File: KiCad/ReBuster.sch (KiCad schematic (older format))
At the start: 11 parts, among them U3 SN74CBTD16210, U4 SN74LVC16T245DGVR, U5 SN74CBTD16210, U6 SN74CBTD16210, U7 74LVC2T45DC, U8 PLCC_84_plug, U9 PLCC_84_plug

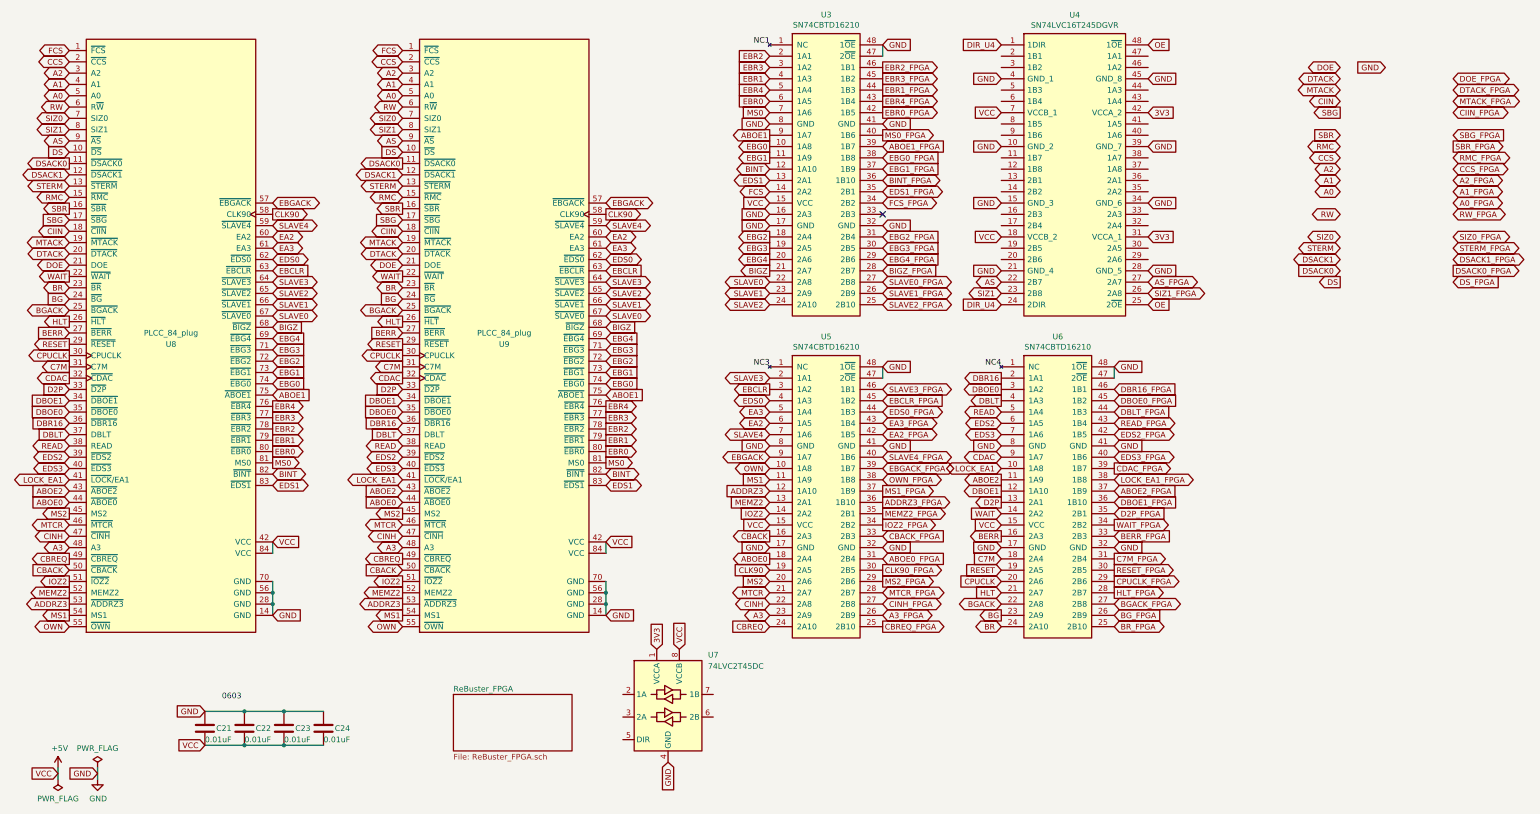
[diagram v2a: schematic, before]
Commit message: Route AS,SIZ1,SIZ0,RW to U4 (SN74LVC16T245DGVR) and FPGA
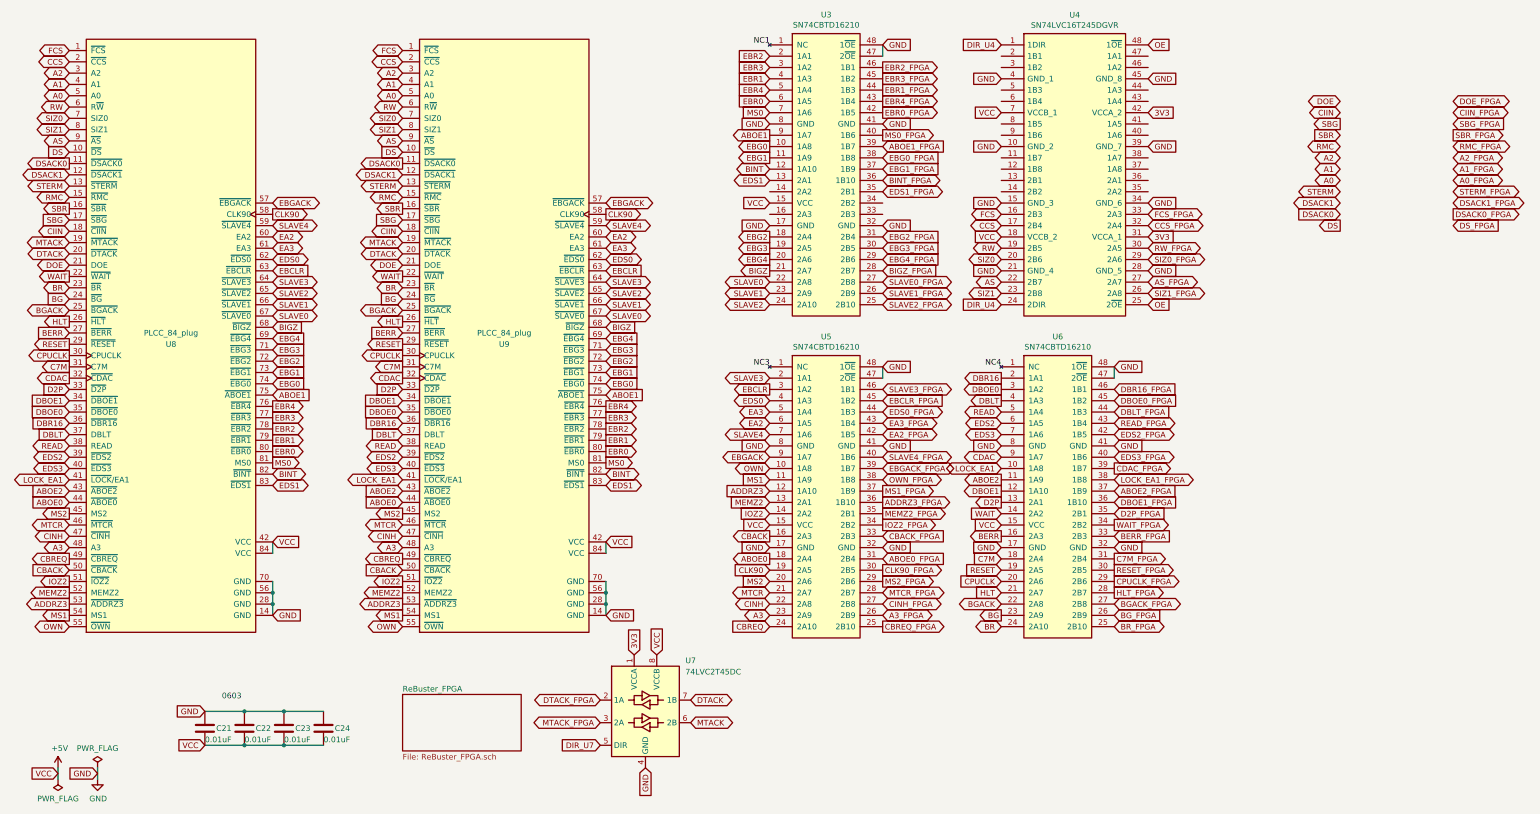
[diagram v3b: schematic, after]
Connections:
- net CCS: now also U4.17 (2B4)
- net CCS_FPGA: now also U4.32 (2A4)
- net DTACK: now also U7.7 (1B)
- net DTACK_FPGA: now also U7.2 (1A)
- net FCS: now also U4.16 (2B3); no longer U3.14 (2A2)
- net FCS_FPGA: now also U4.33 (2A3); no longer U3.34 (2B2)
- net GND: no longer U3.16 (2A3)
- net MTACK: now also U7.6 (2B)
- net MTACK_FPGA: now also U7.3 (2A)
- net RW: now also U4.19 (2B5)
- net RW_FPGA: now also U4.30 (2A5)
- net SIZ0: now also U4.20 (2B6)
- net SIZ0_FPGA: now also U4.29 (2A6)
- net DIR_U7: now reaches U7.5 (DIR)
- no-connect marks 1 -> 0
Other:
- moved on the sheet: U7
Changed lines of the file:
@@
 Wire Wire Line
 	8150 3900 8150 3800
-$Comp
-L ReBuster:SN74CBTD16210 U3
-U 1 1 6058DC08
-P 7650 2050
-F 0 "U3" H 7650 3417 50  0000 C CNN
-F 1 "SN74CBTD16210" H 7650 3326 50  0000 C CNN
-F 2 "ReBuster:TSSOP-48_6.1x12.5mm_P0.5mm_padLength_1mm" H 9300 2500 50  0001 C CNN
-F 3 "https://www.ti.com/lit/ds/symlink/sn74cbtd16210.pdf" H 9300 2500 50  0001 C CNN
-	1    7650 2050
-	1    0    0    -1
-$EndComp
 Text GLabel 8150 1650 2    50   Input ~ 0
 GND
@@
 Text GLabel 8150 2250 2    50   BiDi ~ 0
 EDS1_FPGA
-Text GLabel 8150 2350 2    50   BiDi ~ 0
+Text GLabel 10500 2450 2    50   BiDi ~ 0
 FCS_FPGA
 Text GLabel 8150 2650 2    50   Input ~ 0
@@
 Text GLabel 10200 5200 2    50   Output ~ 0
 WAIT_FPGA
-Text GLabel 13200 1250 2    50   BiDi ~ 0
+Text GLabel 13200 1450 2    50   BiDi ~ 0
 DOE_FPGA
-Text GLabel 13200 1350 2    50   BiDi ~ 0
+Text GLabel 5650 6750 0    50   BiDi ~ 0
 DTACK_FPGA
-Text GLabel 13200 1450 2    50   BiDi ~ 0
+Text GLabel 5650 6950 0    50   BiDi ~ 0
 MTACK_FPGA
 Text GLabel 13200 1550 2    50   BiDi ~ 0
 CIIN_FPGA
-Text GLabel 13200 1850 2    50   Output ~ 0
+Text GLabel 13200 1750 2    50   Output ~ 0
 SBR_FPGA
+Text GLabel 13200 1850 2    50   BiDi ~ 0
+RMC_FPGA
+Text GLabel 10500 2550 2    50   BiDi ~ 0
+CCS_FPGA
 Text GLabel 13200 1950 2    50   BiDi ~ 0
-RMC_FPGA
+A2_FPGA
 Text GLabel 13200 2050 2    50   BiDi ~ 0
-CCS_FPGA
-Text GLabel 13200 2150 2    50   BiDi ~ 0
-A2_FPGA
+A1_FPGA
+Text GLabel 13200 1650 2    50   Input ~ 0
+SBG_FPGA
+Text GLabel 10500 2750 2    50   BiDi ~ 0
+RW_FPGA
+Text GLabel 10500 2850 2    50   BiDi ~ 0
+SIZ0_FPGA
 Text GLabel 13200 2250 2    50   BiDi ~ 0
-A1_FPGA
-Text GLabel 13200 1750 2    50   Input ~ 0
-SBG_FPGA
-Text GLabel 13200 2450 2    50   BiDi ~ 0
-RW_FPGA
-Text GLabel 13200 2650 2    50   BiDi ~ 0
-SIZ0_FPGA
-Text GLabel 13200 2750 2    50   BiDi ~ 0
 STERM_FPGA
-Text GLabel 13200 3050 2    50   Input ~ 0
+Text GLabel 13200 2550 2    50   Input ~ 0
 DS_FPGA
 Text GLabel 10500 3050 2    50   BiDi ~ 0
@@
 SLAVE4_FPGA
 $Sheet
-S 4350 6700 1050 500
+S 3900 6700 1050 500
 U 608A10F5
 F0 "ReBuster_FPGA" 50
 F1 "ReBuster_FPGA.sch" 50
 $EndSheet
-Text GLabel 7150 2250 0    50   BiDi ~ 0
+Text GLabel 9200 2450 0    50   BiDi ~ 0
 FCS
+Text GLabel 9200 2550 0    50   BiDi ~ 0
+CCS
 Text GLabel 12200 1950 0    50   BiDi ~ 0
-CCS
+A2
 Text GLabel 12200 2050 0    50   BiDi ~ 0
-A2
+A1
 Text GLabel 12200 2150 0    50   BiDi ~ 0
-A1
-Text GLabel 12200 2250 0    50   BiDi ~ 0
 A0
-Text GLabel 12200 2450 0    50   BiDi ~ 0
+Text GLabel 9200 2750 0    50   BiDi ~ 0
 RW
-Text GLabel 12200 2650 0    50   BiDi ~ 0
+Text GLabel 9200 2850 0    50   BiDi ~ 0
 SIZ0
 Text GLabel 9200 3150 0    50   BiDi ~ 0
@@
 Text GLabel 9200 3050 0    50   BiDi ~ 0
 AS
-Text GLabel 12200 3050 0    50   Output ~ 0
+Text GLabel 12200 2550 0    50   Output ~ 0
 DS
-Text GLabel 12200 2950 0    50   Input ~ 0
+Text GLabel 12200 2450 0    50   Input ~ 0
 DSACK0
-Text GLabel 12200 2850 0    50   BiDi ~ 0
+Text GLabel 12200 2350 0    50   BiDi ~ 0
 DSACK1
-Text GLabel 12200 2750 0    50   BiDi ~ 0
+Text GLabel 12200 2250 0    50   BiDi ~ 0
 STERM
 Wire Wire Line
@@
 Text GLabel 12200 1750 0    50   Input ~ 0
 SBR
-Text GLabel 12200 1550 0    50   Output ~ 0
+Text GLabel 12200 1650 0    50   Output ~ 0
 SBG
+Text GLabel 12200 1550 0    50   BiDi ~ 0
+CIIN
+Wire Wire Line
+	2750 5350 2750 5450
+Text GLabel 6450 6950 2    50   BiDi ~ 0
+MTACK
+Text GLabel 6450 6750 2    50   BiDi ~ 0
+DTACK
 Text GLabel 12200 1450 0    50   BiDi ~ 0
-CIIN
-Wire Wire Line
-	2750 5350 2750 5450
-Text GLabel 12200 1350 0    50   BiDi ~ 0
-MTACK
-Text GLabel 12200 1250 0    50   BiDi ~ 0
-DTACK
-Text GLabel 12200 1150 0    50   BiDi ~ 0
 DOE
 Text GLabel 9200 5100 0    50   Input ~ 0
@@
 Wire Wire Line
 	5700 5900 5700 6000
-Text GLabel 12600 1150 0    50   Input ~ 0
-GND
-Text GLabel 7150 2450 0    50   Input ~ 0
-GND
 Text GLabel 8150 1550 2    50   Output ~ 0
 EBR0_FPGA
-NoConn ~ 8150 2450
+Text GLabel 13200 2150 2    50   BiDi ~ 0
+A0_FPGA
 Text GLabel 13200 2350 2    50   BiDi ~ 0
-A0_FPGA
-Text GLabel 13200 2850 2    50   BiDi ~ 0
 DSACK1_FPGA
-Text GLabel 13200 2950 2    50   Output ~ 0
+Text GLabel 13200 2450 2    50   Output ~ 0
 DSACK0_FPGA
 $Comp
@@
 L Logic_LevelTranslator:74LVC2T45DC U7
 U 1 1 69AF9BA6
-P 6250 6800
-F 0 "U7" H 6650 7250 50  0000 C CNN
-F 1 "74LVC2T45DC" H 6850 7150 50  0000 C CNN
-F 2 "Package_SO:VSSOP-8_2.3x2mm_P0.5mm" H 6250 5950 50  0001 C CNN
-F 3 "https://assets.nexperia.com/documents/data-sheet/74LVC_LVCH2T45.pdf" H 6500 6550 50  0001 C CNN
-	1    6250 6800
+P 6050 6850
+F 0 "U7" H 6450 7300 50  0000 C CNN
+F 1 "74LVC2T45DC" H 6650 7200 50  0000 C CNN
+F 2 "Package_SO:VSSOP-8_2.3x2mm_P0.5mm" H 6050 6000 50  0001 C CNN
+F 3 "https://assets.nexperia.com/documents/data-sheet/74LVC_LVCH2T45.pdf" H 6300 6600 50  0001 C CNN
+	1    6050 6850
 	1    0    0    -1
 $EndComp
-Text GLabel 6150 6300 1    50   Input ~ 0
+Text GLabel 5950 6350 1    50   Input ~ 0
 3V3
-Text GLabel 6350 6300 1    50   Input ~ 0
+Text GLabel 6150 6350 1    50   Input ~ 0
 VCC
-Text GLabel 6250 7300 3    50   Input ~ 0
-GND
+Text GLabel 6050 7350 3    50   Input ~ 0
+GND
+Text GLabel 5650 7150 0    50   Input ~ 0
+DIR_U7
+$Comp
+L ReBuster:SN74CBTD16210 U3
+U 1 1 6058DC08
+P 7650 2050
+F 0 "U3" H 7650 3417 50  0000 C CNN
+F 1 "SN74CBTD16210" H 7650 3326 50  0000 C CNN
+F 2 "ReBuster:TSSOP-48_6.1x12.5mm_P0.5mm_padLength_1mm" H 9300 2500 50  0001 C CNN
+F 3 "https://www.ti.com/lit/ds/symlink/sn74cbtd16210.pdf" H 9300 2500 50  0001 C CNN
+	1    7650 2050
+	1    0    0    -1
+$EndComp
 $EndSCHEMATC

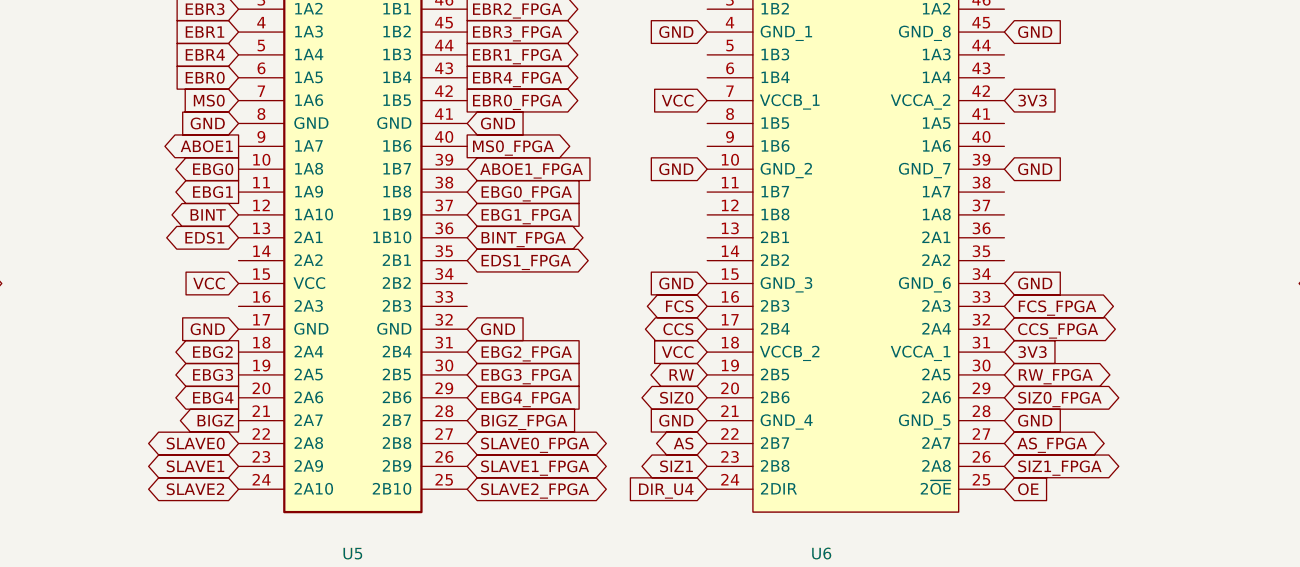
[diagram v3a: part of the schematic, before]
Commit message: Route EDS1, CCS, FCS signals to U4 (SN74LVC16T245DGVR) and FPGA
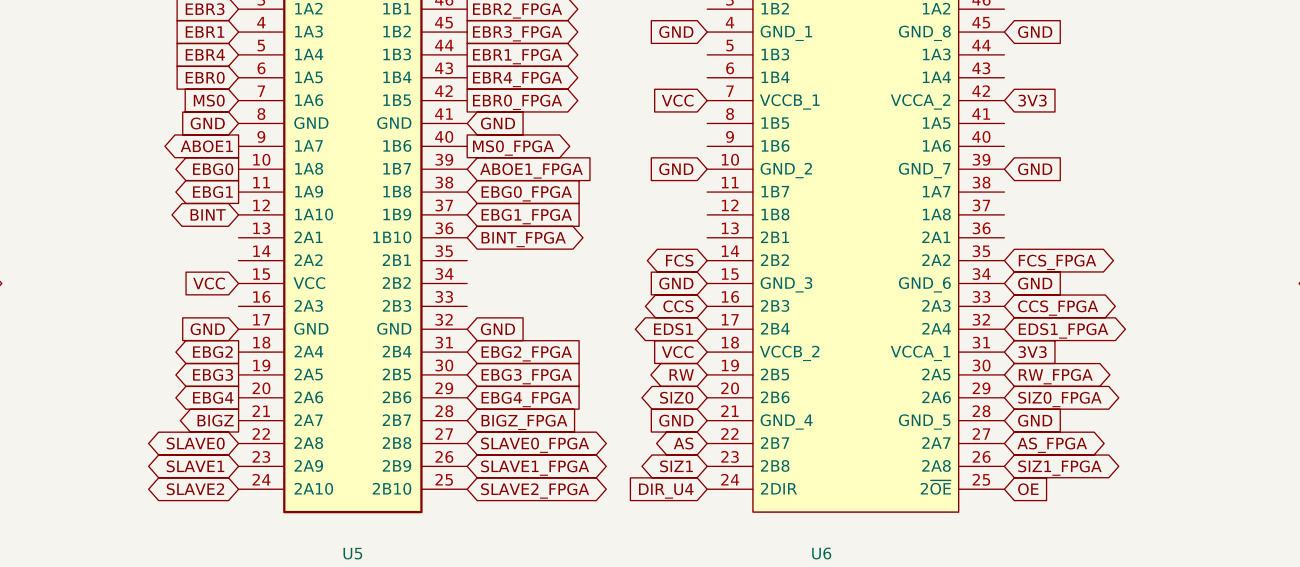
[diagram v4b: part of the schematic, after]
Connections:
- net CCS: now also U4.16 (2B3); no longer U4.17 (2B4)
- net CCS_FPGA: now also U4.33 (2A3); no longer U4.32 (2A4)
- net EDS1: now also U4.17 (2B4); no longer U3.13 (2A1)
- net EDS1_FPGA: now also U4.32 (2A4); no longer U3.35 (2B1)
- net FCS: now also U4.14 (2B2); no longer U4.16 (2B3)
- net FCS_FPGA: now also U4.35 (2A2); no longer U4.33 (2A3)
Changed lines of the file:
@@
 Text GLabel 8150 2050 2    50   Input ~ 0
 EBG1_FPGA
-Text GLabel 8150 2250 2    50   BiDi ~ 0
+Text GLabel 10500 2550 2    50   BiDi ~ 0
 EDS1_FPGA
-Text GLabel 10500 2450 2    50   BiDi ~ 0
+Text GLabel 10500 2250 2    50   BiDi ~ 0
 FCS_FPGA
 Text GLabel 8150 2650 2    50   Input ~ 0
@@
 Text GLabel 13200 1850 2    50   BiDi ~ 0
 RMC_FPGA
-Text GLabel 10500 2550 2    50   BiDi ~ 0
+Text GLabel 10500 2450 2    50   BiDi ~ 0
 CCS_FPGA
 Text GLabel 13200 1950 2    50   BiDi ~ 0
@@
 F1 "ReBuster_FPGA.sch" 50
 $EndSheet
+Text GLabel 9200 2250 0    50   BiDi ~ 0
+FCS
 Text GLabel 9200 2450 0    50   BiDi ~ 0
-FCS
-Text GLabel 9200 2550 0    50   BiDi ~ 0
 CCS
 Text GLabel 12200 1950 0    50   BiDi ~ 0
@@
 Text GLabel 7150 4200 0    50   BiDi ~ 0
 EA3
-Text GLabel 7150 2150 0    50   BiDi ~ 0
+Text GLabel 9200 2550 0    50   BiDi ~ 0
 EDS1
 Text GLabel 7150 2050 0    50   BiDi ~ 0

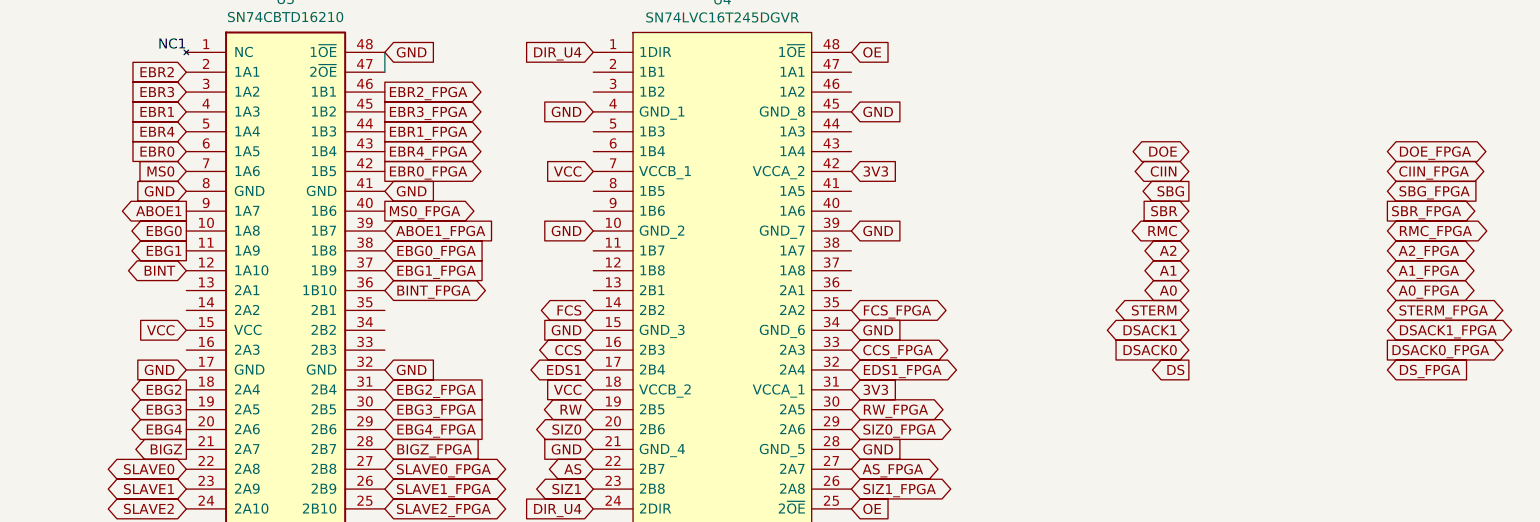
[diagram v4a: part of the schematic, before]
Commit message: Relocate A0,A1,A2 to FPGA pin A4,A5,A6 and route traces
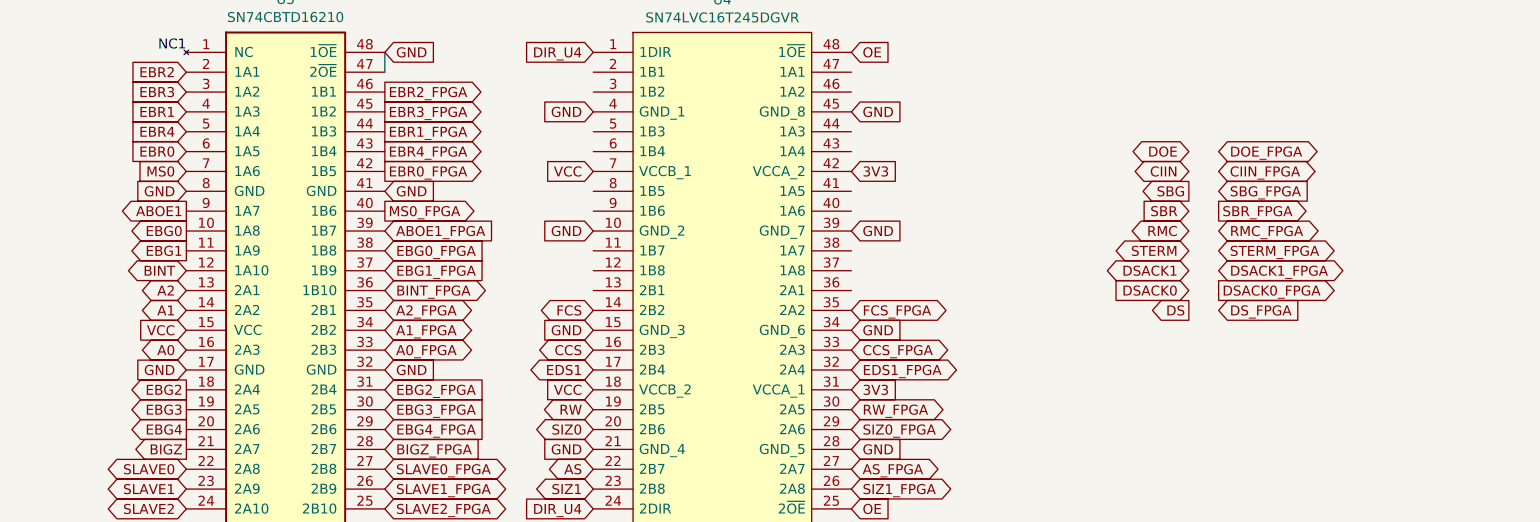
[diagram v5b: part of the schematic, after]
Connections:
- net A0: now also U3.16 (2A3)
- net A0_FPGA: now also U3.33 (2B3)
- net A1: now also U3.14 (2A2)
- net A1_FPGA: now also U3.34 (2B2)
- net A2: now also U3.13 (2A1)
- net A2_FPGA: now also U3.35 (2B1)
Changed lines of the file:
@@
 Text GLabel 10200 5200 2    50   Output ~ 0
 WAIT_FPGA
-Text GLabel 13200 1450 2    50   BiDi ~ 0
+Text GLabel 12350 1450 2    50   BiDi ~ 0
 DOE_FPGA
 Text GLabel 5650 6750 0    50   BiDi ~ 0
@@
 Text GLabel 5650 6950 0    50   BiDi ~ 0
 MTACK_FPGA
-Text GLabel 13200 1550 2    50   BiDi ~ 0
+Text GLabel 12350 1550 2    50   BiDi ~ 0
 CIIN_FPGA
-Text GLabel 13200 1750 2    50   Output ~ 0
+Text GLabel 12350 1750 2    50   Output ~ 0
 SBR_FPGA
-Text GLabel 13200 1850 2    50   BiDi ~ 0
+Text GLabel 12350 1850 2    50   BiDi ~ 0
 RMC_FPGA
 Text GLabel 10500 2450 2    50   BiDi ~ 0
 CCS_FPGA
-Text GLabel 13200 1950 2    50   BiDi ~ 0
+Text GLabel 8150 2250 2    50   BiDi ~ 0
 A2_FPGA
-Text GLabel 13200 2050 2    50   BiDi ~ 0
+Text GLabel 8150 2350 2    50   BiDi ~ 0
 A1_FPGA
-Text GLabel 13200 1650 2    50   Input ~ 0
+Text GLabel 12350 1650 2    50   Input ~ 0
 SBG_FPGA
 Text GLabel 10500 2750 2    50   BiDi ~ 0
@@
 Text GLabel 10500 2850 2    50   BiDi ~ 0
 SIZ0_FPGA
-Text GLabel 13200 2250 2    50   BiDi ~ 0
+Text GLabel 12350 1950 2    50   BiDi ~ 0
 STERM_FPGA
-Text GLabel 13200 2550 2    50   Input ~ 0
+Text GLabel 12350 2250 2    50   Input ~ 0
 DS_FPGA
 Text GLabel 10500 3050 2    50   BiDi ~ 0
@@
 Text GLabel 9200 2450 0    50   BiDi ~ 0
 CCS
-Text GLabel 12200 1950 0    50   BiDi ~ 0
+Text GLabel 7150 2150 0    50   BiDi ~ 0
 A2
-Text GLabel 12200 2050 0    50   BiDi ~ 0
+Text GLabel 7150 2250 0    50   BiDi ~ 0
 A1
-Text GLabel 12200 2150 0    50   BiDi ~ 0
+Text GLabel 7150 2450 0    50   BiDi ~ 0
 A0
 Text GLabel 9200 2750 0    50   BiDi ~ 0
@@
 Text GLabel 9200 3050 0    50   BiDi ~ 0
 AS
-Text GLabel 12200 2550 0    50   Output ~ 0
+Text GLabel 12200 2250 0    50   Output ~ 0
 DS
-Text GLabel 12200 2450 0    50   Input ~ 0
+Text GLabel 12200 2150 0    50   Input ~ 0
 DSACK0
-Text GLabel 12200 2350 0    50   BiDi ~ 0
+Text GLabel 12200 2050 0    50   BiDi ~ 0
 DSACK1
-Text GLabel 12200 2250 0    50   BiDi ~ 0
+Text GLabel 12200 1950 0    50   BiDi ~ 0
 STERM
 Wire Wire Line
@@
 Text GLabel 8150 1550 2    50   Output ~ 0
 EBR0_FPGA
-Text GLabel 13200 2150 2    50   BiDi ~ 0
+Text GLabel 8150 2450 2    50   BiDi ~ 0
 A0_FPGA
-Text GLabel 13200 2350 2    50   BiDi ~ 0
+Text GLabel 12350 2050 2    50   BiDi ~ 0
 DSACK1_FPGA
-Text GLabel 13200 2450 2    50   Output ~ 0
+Text GLabel 12350 2150 2    50   Output ~ 0
 DSACK0_FPGA
 $Comp
